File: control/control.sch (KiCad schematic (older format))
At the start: 87 parts, among them M1 LMR62014, M2 LM46001, M3 STM32F4XX, M4 TPS736XX, M5 SN65HVD23X, P1 GND/VDD, P2 VOLTAGE, P3 INTERFACE, P4 POWER/FETS, P5 SENSOR_A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

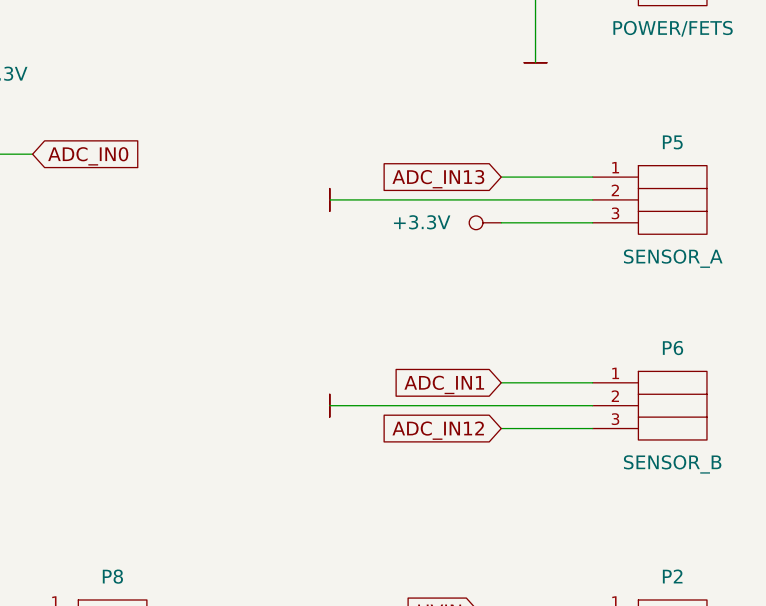
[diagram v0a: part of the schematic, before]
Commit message: Replaced ACS7XX sensors to the current shunt amplifiers.
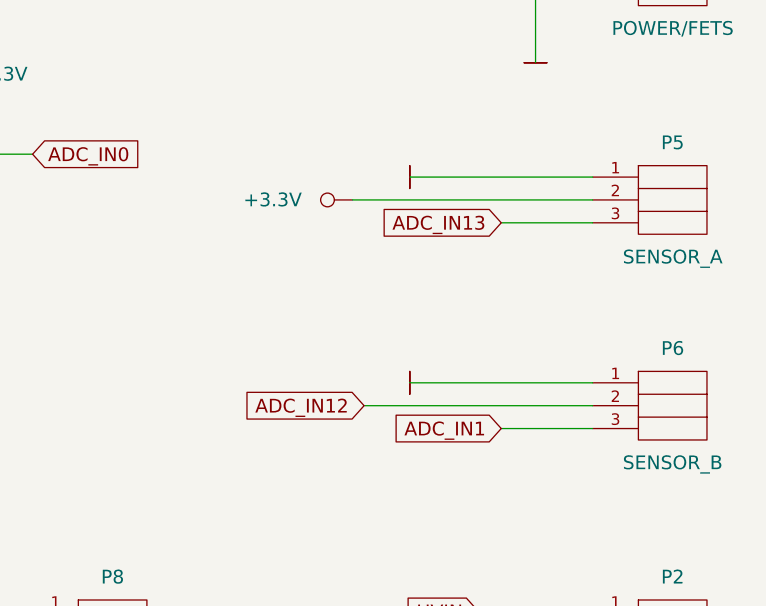
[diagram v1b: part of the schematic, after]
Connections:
- net +3.3V: now also P5.2; no longer P5.3
- net ADC_IN1: now also P6.3; no longer P6.1
- net ADC_IN12: now also P6.2; no longer P6.3
- net ADC_IN13: now also P5.3; no longer P5.1
- net GND: now also P5.1, P6.1; no longer P5.2, P6.2
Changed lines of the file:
@@
 L GND #PWR07
 U 1 1 5686AEC2
-P 13900 3100
-F 0 "#PWR07" H 13900 3100 30  0001 C CNN
-F 1 "GND" H 13900 3030 30  0001 C CNN
-F 2 "" H 13900 3100 60  0000 C CNN
-F 3 "" H 13900 3100 60  0000 C CNN
-	1    13900 3100
+P 14250 3000
+F 0 "#PWR07" H 14250 3000 30  0001 C CNN
+F 1 "GND" H 14250 2930 30  0001 C CNN
+F 2 "" H 14250 3000 60  0000 C CNN
+F 3 "" H 14250 3000 60  0000 C CNN
+	1    14250 3000
 	0    1    1    0
 $EndComp
@@
 Text GLabel 12600 1550 2    60   Input ~ 0
 ADC_IN2
-Text GLabel 14650 3000 0    60   Input ~ 0
+Text GLabel 14650 3200 0    60   Input ~ 0
 ADC_IN13
-Text GLabel 14650 3900 0    60   Input ~ 0
+Text GLabel 14650 4100 0    60   Input ~ 0
 ADC_IN1
 $Comp
@@
 L +3.3V #PWR038
 U 1 1 5699D8BB
-P 14650 3200
-F 0 "#PWR038" H 14650 3290 20  0001 C CNN
-F 1 "+3.3V" V 14650 3550 60  0000 C CNN
-F 2 "" H 14650 3200 60  0000 C CNN
-F 3 "" H 14650 3200 60  0000 C CNN
-	1    14650 3200
+P 14000 3100
+F 0 "#PWR038" H 14000 3190 20  0001 C CNN
+F 1 "+3.3V" V 14000 3450 60  0000 C CNN
+F 2 "" H 14000 3100 60  0000 C CNN
+F 3 "" H 14000 3100 60  0000 C CNN
+	1    14000 3100
 	0    -1   -1   0
 $EndComp
@@
 Text GLabel 5750 7700 0    60   Input ~ 0
 ADC_IN12
-Text GLabel 14650 4100 0    60   Input ~ 0
+Text GLabel 14050 4000 0    60   Input ~ 0
 ADC_IN12
 $Comp
@@
 	6300 8700 6500 8700
 Wire Wire Line
-	13900 4000 15050 4000
-Wire Wire Line
 	5750 7700 6500 7700
 Wire Wire Line
@@
 Wire Wire Line
 	11500 1650 11500 2100
-Wire Wire Line
-	14650 4100 15050 4100
 Wire Wire Line
 	6500 8200 6300 8200
@@
 	15050 3200 14650 3200
 Wire Wire Line
-	15050 3900 14650 3900
-Wire Wire Line
-	15050 3000 14650 3000
-Wire Wire Line
-	15050 3100 13900 3100
+	14250 3900 15050 3900
+Wire Wire Line
+	14250 3000 15050 3000
 Wire Wire Line
 	15050 1500 14200 1500
@@
 Connection ~ 12450 6400
 $Comp
-L GND #PWR?
+L GND #PWR053
 U 1 1 56FBF8E3
-P 13900 4000
-F 0 "#PWR?" H 13900 4000 30  0001 C CNN
-F 1 "GND" H 13900 3930 30  0001 C CNN
-F 2 "" H 13900 4000 60  0000 C CNN
-F 3 "" H 13900 4000 60  0000 C CNN
-	1    13900 4000
+P 14250 3900
+F 0 "#PWR053" H 14250 3900 30  0001 C CNN
+F 1 "GND" H 14250 3830 30  0001 C CNN
+F 2 "" H 14250 3900 60  0000 C CNN
+F 3 "" H 14250 3900 60  0000 C CNN
+	1    14250 3900
 	0    1    1    0
 $EndComp
+Wire Wire Line
+	15050 3100 14000 3100
+Wire Wire Line
+	14050 4000 15050 4000
+Wire Wire Line
+	14650 4100 15050 4100
 $EndSCHEMATC

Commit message: Fixed a few small mistakes.
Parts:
- C6: value 100nF -> 10nF
- C8: value 10nF -> 100nF
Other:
- moved on the sheet: C6, C8
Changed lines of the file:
@@
 L C C6
 U 1 1 5686AEEA
+P 4850 9200
+F 0 "C6" V 4950 9450 60  0000 C CNN
+F 1 "10nF" V 4750 9450 60  0000 C CNN
+F 2 "foot:SM0603" H 4850 9200 60  0001 C CNN
+F 3 "" H 4850 9200 60  0000 C CNN
+	1    4850 9200
+	0    -1   -1   0
+$EndComp
+$Comp
+L C C8
+U 1 1 5686AEEB
 P 4300 9200
-F 0 "C6" V 4400 9450 60  0000 C CNN
+F 0 "C8" V 4400 9450 60  0000 C CNN
 F 1 "100nF" V 4200 9450 60  0000 C CNN
 F 2 "foot:SM0603" H 4300 9200 60  0001 C CNN
@@
 	0    -1   -1   0
 $EndComp
-$Comp
-L C C8
-U 1 1 5686AEEB
-P 4850 9200
-F 0 "C8" V 4950 9450 60  0000 C CNN
-F 1 "10nF" V 4750 9450 60  0000 C CNN
-F 2 "foot:SM0603" H 4850 9200 60  0001 C CNN
-F 3 "" H 4850 9200 60  0000 C CNN
-	1    4850 9200
-	0    -1   -1   0
-$EndComp

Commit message: Added revison 3.
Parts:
- removed M1: LMR62014, foot:SOT23-5, symbol LMR62014
- removed P8: ANALOG, foot:PLS2, symbol PLS_2
- added C46: 100nF, foot:SM0603, symbol C
- added M1: TPS61040, foot:SOT23-5, symbol TPS61040
- added M6: REF30XX, foot:SOT23, symbol REF30XX
- added Q1: BC857C, foot:SOT23, symbol BJT-PNP
- C12, C7: value 20pF -> 12pF
- C19: value 10uF -> 100nF; footprint foot:SM1210 -> foot:SM0603
- C24: value 100nF -> 4.7uF; footprint foot:SM0603 -> foot:SM0805
- C26, C28: value 47uF -> 100nF; footprint foot:SM1210 -> foot:SM0603
- C9: value 220pF -> 22pF
- M4: footprint foot:SOT223 -> foot:SOT23-5
- R3: value 270 -> 470
- R4: value 11K -> 11K 1%
- R5, R6: value 100K -> 100K 1%
- R7: value 27K -> 27K 1%
- Z1: value 8MHz -> 12MHz; footprint foot:HC-49US -> foot:SMD_Z3225
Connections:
- net +12V: now also C9.1, P4.10, R5.2, Q1.2 (C); no longer C17.1, C9.2, D1.1, P4.9, R5.1
- net +3.3V: now also R10.1, R12.1, R9.1; no longer C6.1, C8.1, M3.13 (V_DDA), P5.2, R10.2, R12.2, R9.2, U1.8 (VCC), U1.8 (VCC)
- net +36V: now also P4.1; no longer P4.2
- net +5V: now also R1.1, M1.5 (VIN), M6.1 (IN); no longer C26.1, C28.1, R1.2
- net EN_A: now also R9.2; no longer R9.1
- net EN_B: now also R12.2; no longer R10.1
- net EN_C: now also R10.2; no longer R12.1
- net FET_AH: now also P4.4; no longer P4.3
- net FET_AL: now also P4.3; no longer P4.4
- net FET_BH: now also P4.6; no longer P4.5
- net FET_BL: now also P4.5; no longer P4.6
- net FET_CH: now also P4.8; no longer P4.7
- net FET_CL: now also P4.7; no longer P4.8
- net GND: now also M4.2 (GND), P4.2, P4.9, C46.2, M1.2 (GND), M6.3 (GND); no longer P4.1, P4.10
- net 12V_EN: now reaches M3.28 (PB2/BOOT1), R8.2
- net 12V_EN: now also M1.4 (EN)
- net at D1.2, L1.2: now also M1.1 (SW)
- net ADC_IN0 renamed ADC_E
- net ADC_IN1 renamed ADC_B
- net ADC_IN12 renamed ADC_NTC
- net ADC_IN13 renamed ADC_A
- net ADC_IN2 renamed ADC_U
- net ADC_IN3: no longer names the net of M3.17 (PA3/ADC_IN3)
- net DAC_OUT1 renamed DAC_B
- net DAC_OUT2 renamed DAC_A
- net LED_BLUE renamed LED_B
- net LED_GREEN renamed LED_G
- net LED_RED renamed LED_R
- net SWDCLK renamed SWCLK
- new net: C17.1, D1.1, Q1.3 (E)
- new net: C9.2, M1.3 (FB), R4.2, R5.1
- new net: Q1.1 (B), R1.2
- new net +3.3VREF: C26.1, C28.1, C46.1, C6.1, C8.1, M3.13 (V_DDA), M6.2 (OUT), P5.2, U1.8 (VCC), U1.8 (VCC)
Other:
- moved on the sheet: C1, C12, C13, C15, C16, C17, C18, C20, C21, C22, C23, C25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

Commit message: Fixed a little mistake.
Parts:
- C9: value 22pF -> 180pF
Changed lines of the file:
@@
 P 5100 4300
 F 0 "C9" V 5200 4100 60  0000 C CNN
-F 1 "22pF" V 5000 4050 60  0000 C CNN
+F 1 "180pF" V 5000 4050 60  0000 C CNN
 F 2 "foot:SM0603" H 5100 4300 60  0001 C CNN
 F 3 "" H 5100 4300 60  0000 C CNN
